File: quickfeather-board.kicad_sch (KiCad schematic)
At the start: 101 parts, among them IC1 EOS-S3-QFN, J1 61300211121, J2 1x12_pinhead, J3 1x16_pinhead, J4 S2B-PH-SM4-TB_LF__SN_, J5 0473460001, J6 FTSH-105-01-L-DV-K, J7 61300211121, J8 2x8_pinhead, M1 mounting_pad, M2 mounting_pad, M3 mounting_pad, M4 mounting_pad, Q1 NX3008CBKV, Q2 2N7002PV, Q3 2N7002PV, Q4 DMG1012T-7, U1 TPS62821DLCR, U2 MCP73831T-2ACI_OT, U3 GD25Q16CWIGR, U4 DPS310, U5 MC3635, X1 ECS-_327-12_5-34B-TR

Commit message: [#54927] Globlib
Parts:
- C1, C14, C16, C2, C5: footprint quickfeather-board-footprints:0603-cap -> antmicro-footprints:C_0603_1608Metric; symbol quickfeather-board:C_4u7_0603 -> antmicroCapacitors0603:C_4u7_0603
- C19: footprint quickfeather-board-footprints:0402-cap -> antmicro-footprints:C_0402_1005Metric; symbol quickfeather-board:C_1u_0402 -> antmicroCapacitors0402:C_1u_0402
- C3: footprint quickfeather-board-footprints:0402-cap -> antmicro-footprints:C_0402_1005Metric; symbol quickfeather-board:C_100p_0402 -> antmicroCapacitors0402:C_100p_0402
- C4: footprint quickfeather-board-footprints:0603-cap -> antmicro-footprints:C_0603_1608Metric; symbol quickfeather-board:C_22u_0603 -> antmicroCapacitors0603:C_22u_0603
- C6, C7: footprint quickfeather-board-footprints:0402-cap -> antmicro-footprints:C_0402_1005Metric; symbol quickfeather-board:C_12p_0402 -> antmicroCapacitors0402:C_12p_0402
- D1: footprint quickfeather-board-footprints:SOD-123 -> antmicro-footprints:D_SOD-123; symbol quickfeather-board:MBR0520LT1G -> antmicroDiodesRectifiersSingle:MBR0520LT1G
- D11, D3, D5: footprint quickfeather-board-footprints:SOT-3 -> antmicro-footprints:SOT-3; symbol quickfeather-board:TPD2EUSB30DRTR -> antmicroTVSDiodes:TPD2EUSB30DRTR
- D6: footprint quickfeather-board-footprints:SOD-323-SD05 -> antmicro-footprints:SOD-323; symbol quickfeather-board:SD05C.TCT -> antmicroTVSDiodes:SD05C.TCT
- MIC1: footprint quickfeather-board-footprints:IM69D130 -> antmicro-footprints:IM69D130; symbol quickfeather-board:IM69D130 -> antmicroMicrophones:IM69D130
- N1: footprint quickfeather-board-footprints:oshw-logo -> antmicro-footprints:oshw-logo; symbol quickfeather-board:oshw_logo -> antmicroMechanicalParts:oshw_logo
- Q1: footprint quickfeather-board-footprints:SOT-563 -> antmicro-footprints:SOT-666; symbol quickfeather-board:NX3008CBKV -> antmicroTransistorsFETsMOSFETsArrays:NX3008CBKV
- Q2, Q3: footprint quickfeather-board-footprints:SOT-563 -> antmicro-footprints:SOT-563; symbol quickfeather-board:2N7002PV -> antmicroTransistorsFETsMOSFETsArrays:2N7002PV
- Q4: footprint quickfeather-board-footprints:SOT-523 -> antmicro-footprints:SOT-523; symbol quickfeather-board:DMG1012T-7 -> antmicroTransistorsFETsMOSFETsSingle:DMG1012T-7
- R1: footprint quickfeather-board-footprints:0402-res -> antmicro-footprints:R_0402_1005Metric; symbol quickfeather-board:R_1M5_0402 -> antmicroResistors0402:R_1M5_0402
- R10, R14, R15, R19, R21, R22, R23, R31, R32, R34, R36, R37, R6, R8: footprint quickfeather-board-footprints:0402-res -> antmicro-footprints:R_0402_1005Metric; symbol quickfeather-board:R_10k_0402 -> antmicroResistors0402:R_10k_0402
- R11, R28, R29, R38, R39, R40, R7: footprint quickfeather-board-footprints:0402-res -> antmicro-footprints:R_0402_1005Metric; symbol quickfeather-board:R_22R_0402 -> antmicroResistors0402:R_22R_0402
- R12, R17, R5: footprint quickfeather-board-footprints:0402-res -> antmicro-footprints:R_0402_1005Metric; symbol quickfeather-board:R_100k_0402 -> antmicroResistors0402:R_100k_0402
- R13, R24, R26: footprint quickfeather-board-footprints:0402-res -> antmicro-footprints:R_0402_1005Metric; symbol quickfeather-board:R_100R_0402 -> antmicroResistors0402:R_100R_0402
- R16: footprint quickfeather-board-footprints:0402-res -> antmicro-footprints:R_0402_1005Metric; symbol quickfeather-board:R_200k_0402 -> antmicroResistors0402:R_200k_0402
- R18, R2, R20: footprint quickfeather-board-footprints:0402-res -> antmicro-footprints:R_0402_1005Metric; symbol quickfeather-board:R_4k7_0402 -> antmicroResistors0402:R_4k7_0402
- R25: footprint quickfeather-board-footprints:0402-res -> antmicro-footprints:R_0402_1005Metric; symbol quickfeather-board:R_220R_0402 -> antmicroResistors0402:R_220R_0402
- R27, R3, R9: footprint quickfeather-board-footprints:0402-res -> antmicro-footprints:R_0402_1005Metric; symbol quickfeather-board:R_1k5_0402 -> antmicroResistors0402:R_1k5_0402
- R4: footprint quickfeather-board-footprints:0402-res -> antmicro-footprints:R_0402_1005Metric; symbol quickfeather-board:R_453k_0402 -> antmicroResistors0402:R_453k_0402
- U1: footprint quickfeather-board-footprints:QFN-8_2x1mm -> antmicro-footprints:QFN-8_2x1mm; symbol quickfeather-board:TPS62821DLCR -> antmicroDCDCConverters:TPS62821DLCR
- U3: footprint quickfeather-board-footprints:GD25Q16CWIG -> antmicro-footprints:GD25Q16CWIG; symbol quickfeather-board:GD25Q16CWIGR -> antmicroMemory:GD25Q16CWIGR
- U5: footprint quickfeather-board-footprints:MC3635 -> antmicro-footprints:LGA-10_1.6x1.6mm; symbol quickfeather-board:MC3635 -> antmicroMotionSensorsIMUsInertialMeasurementUnits:MC3635

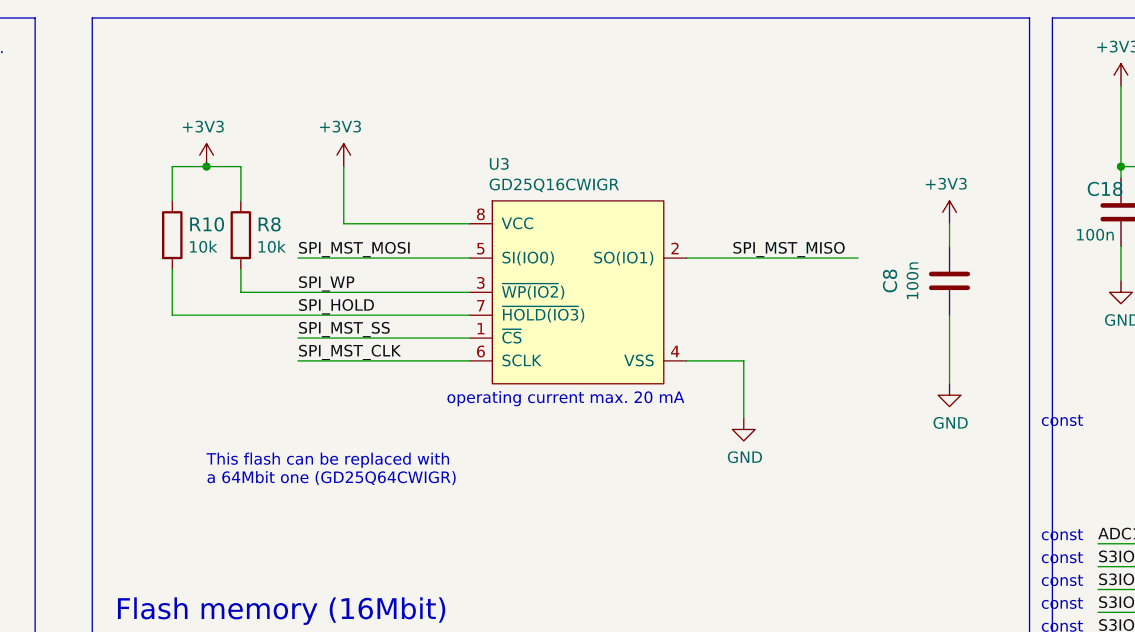
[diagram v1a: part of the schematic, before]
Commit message: [#54927] Update Flash memory
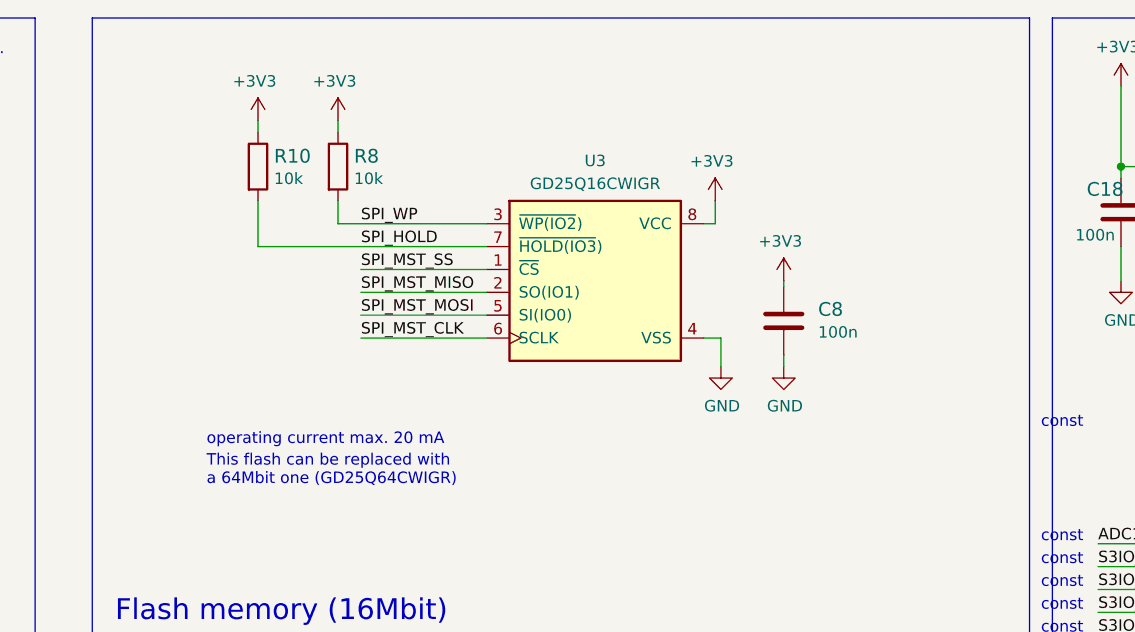
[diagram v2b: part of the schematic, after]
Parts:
- U3: Author (none) -> Antmicro; License (none) -> Apache-2.0
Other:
- moved on the sheet: C8, R10, R8

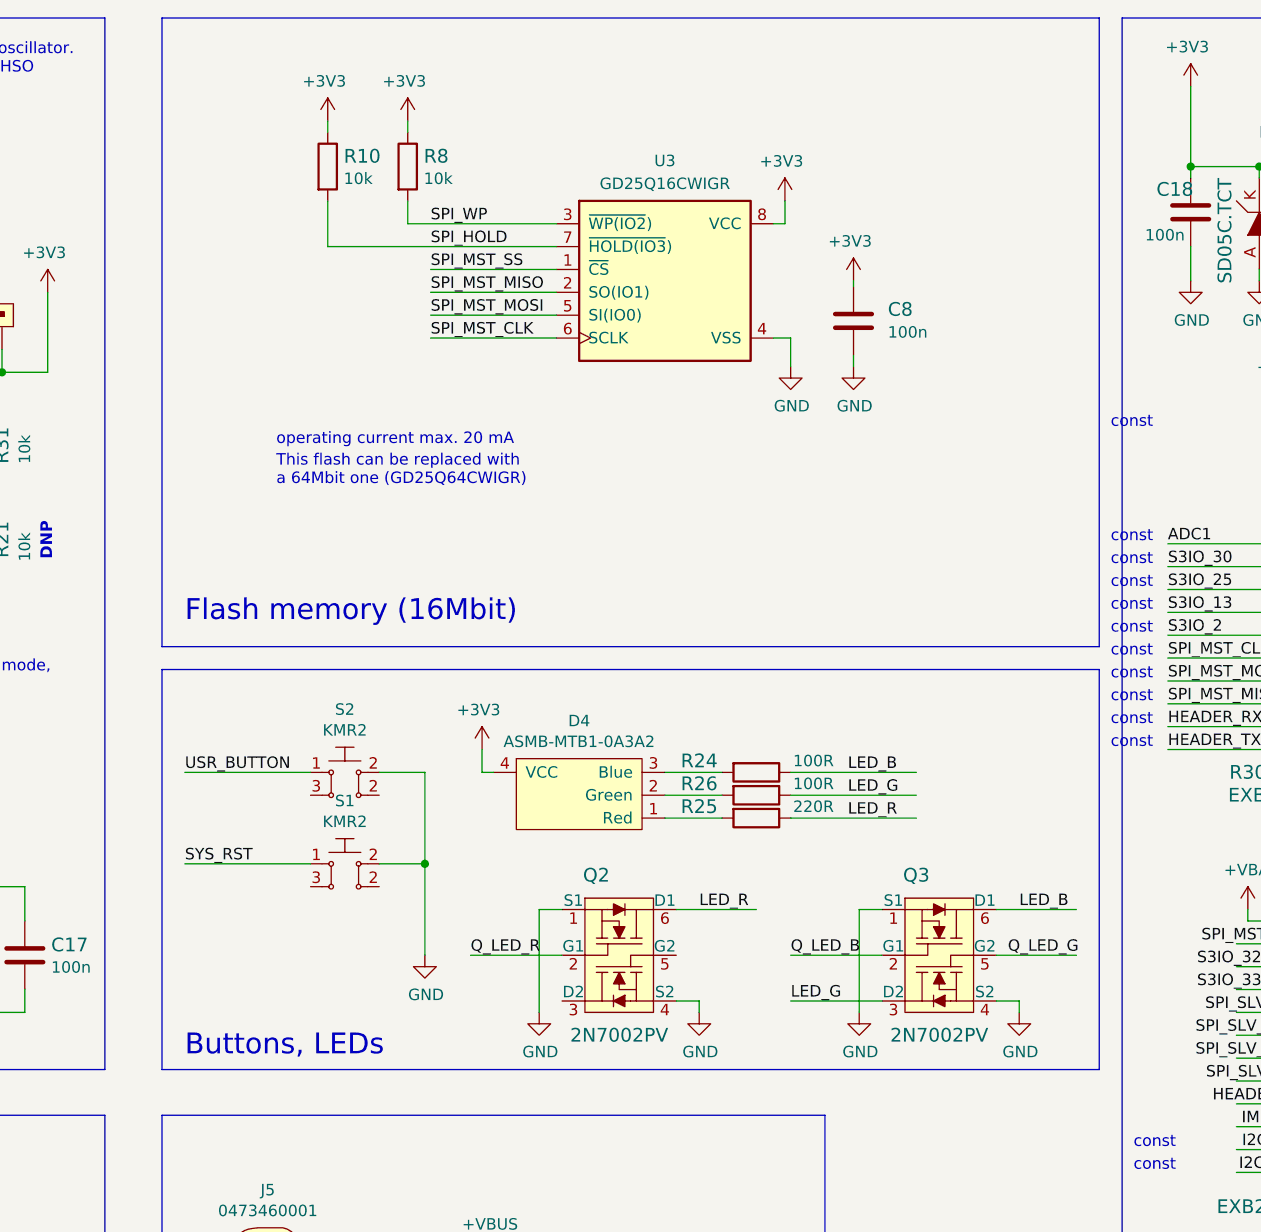
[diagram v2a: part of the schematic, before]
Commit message: [#54927] Standardize USER IO
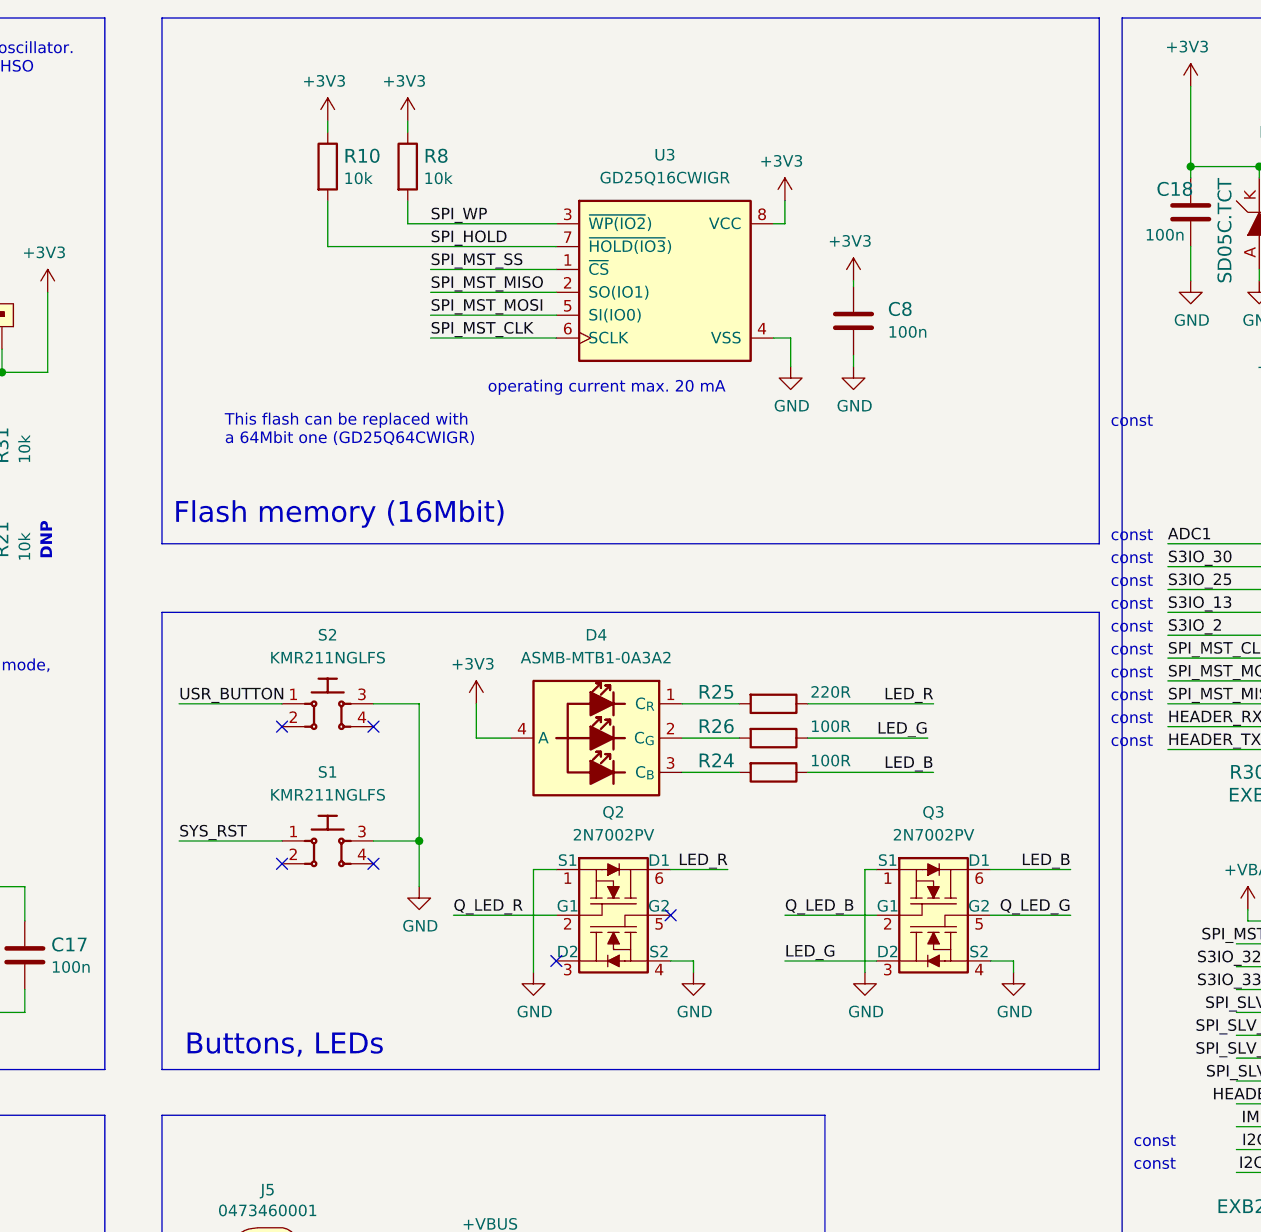
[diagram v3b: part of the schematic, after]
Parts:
- D4: footprint quickfeather-board-footprints:LED-PLCC4_3.2x2.8mm_B -> antmicro-footprints:PLCC4_3.2x2.8mm; symbol quickfeather-board:ASMB-MTB1-0A3A2 -> antmicroLEDIndicationDiscrete:LED_RGB_PLCC4_ASMB_MTB1_0A3A2; Author (none) -> Antmicro; License (none) -> Apache-2.0; MPN UHD1110-FKA -> ASMB-MTB1-0A3A2; Manufacturer Broadcom -> Avago Technologies
- Q2, Q3: Author (none) -> Antmicro; License (none) -> Apache-2.0
- S1, S2: footprint quickfeather-board-footprints:SW_SPST_4.2x2.8 -> antmicro-footprints:SW_KMR211NGLFS_SMD; symbol quickfeather-board:KMR2 -> antmicroPushbuttonSwitches:SW_KMR211NGLFS_SMD; Author (none) -> Antmicro; License (none) -> Apache-2.0; Manufacturer C&K Components -> C&K
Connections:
- net GND: now also S1.3, S2.3; no longer S1.2, S2.2
- no-connect marks 4 -> 10
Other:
- moved on the sheet: Q2, Q3, R24, R25, R26, S1, S2
